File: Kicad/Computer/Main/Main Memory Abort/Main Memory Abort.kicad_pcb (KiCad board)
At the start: 2 copper layers, 18.8 x 43.3 mm, 14 parts, among them IC1 AP7365-33WG-7, IC2 74LVC32APW,118, IC4 74LVC74APW,118, IC5 SN74CBT3257CPWR, IC7 74LVC11PW,112, J2 Conn_02x16_Counter_Clockwise

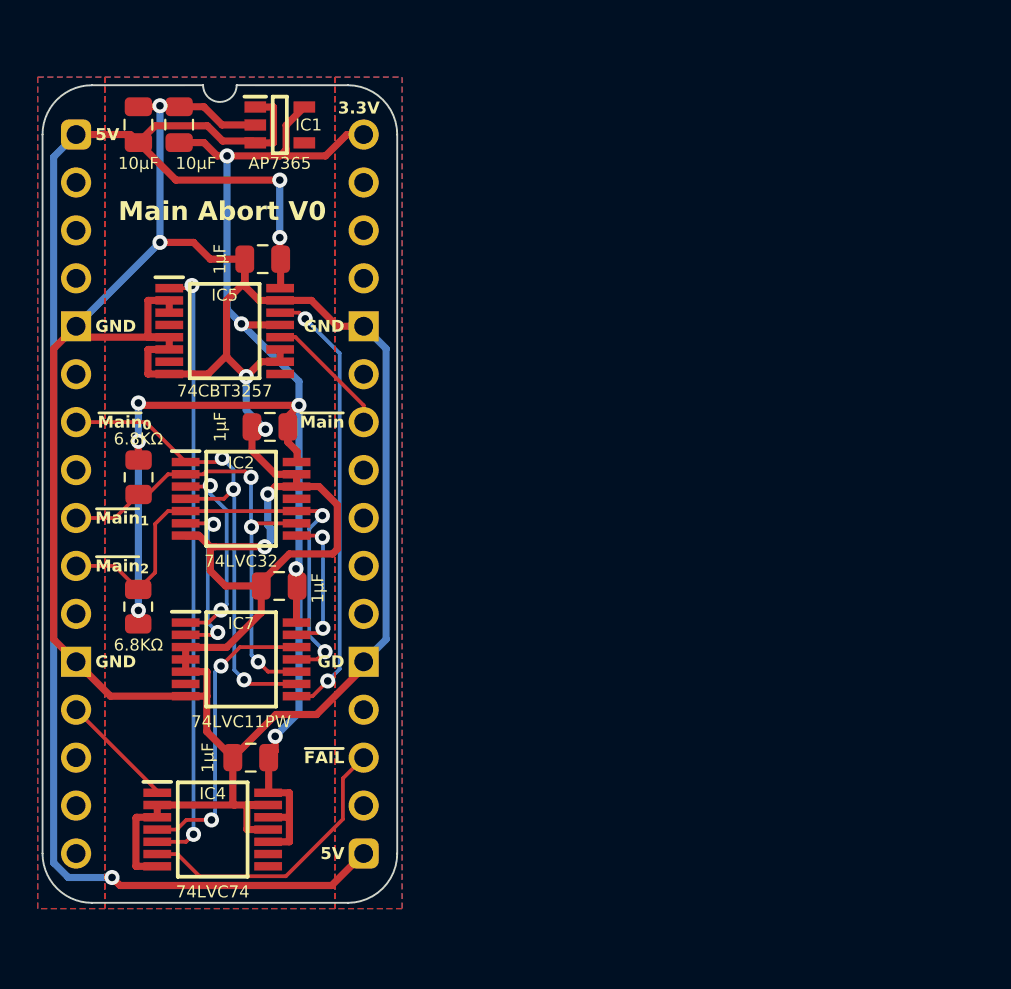
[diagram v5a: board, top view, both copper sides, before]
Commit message: Split Main Memory Abort into Enable and Abort.
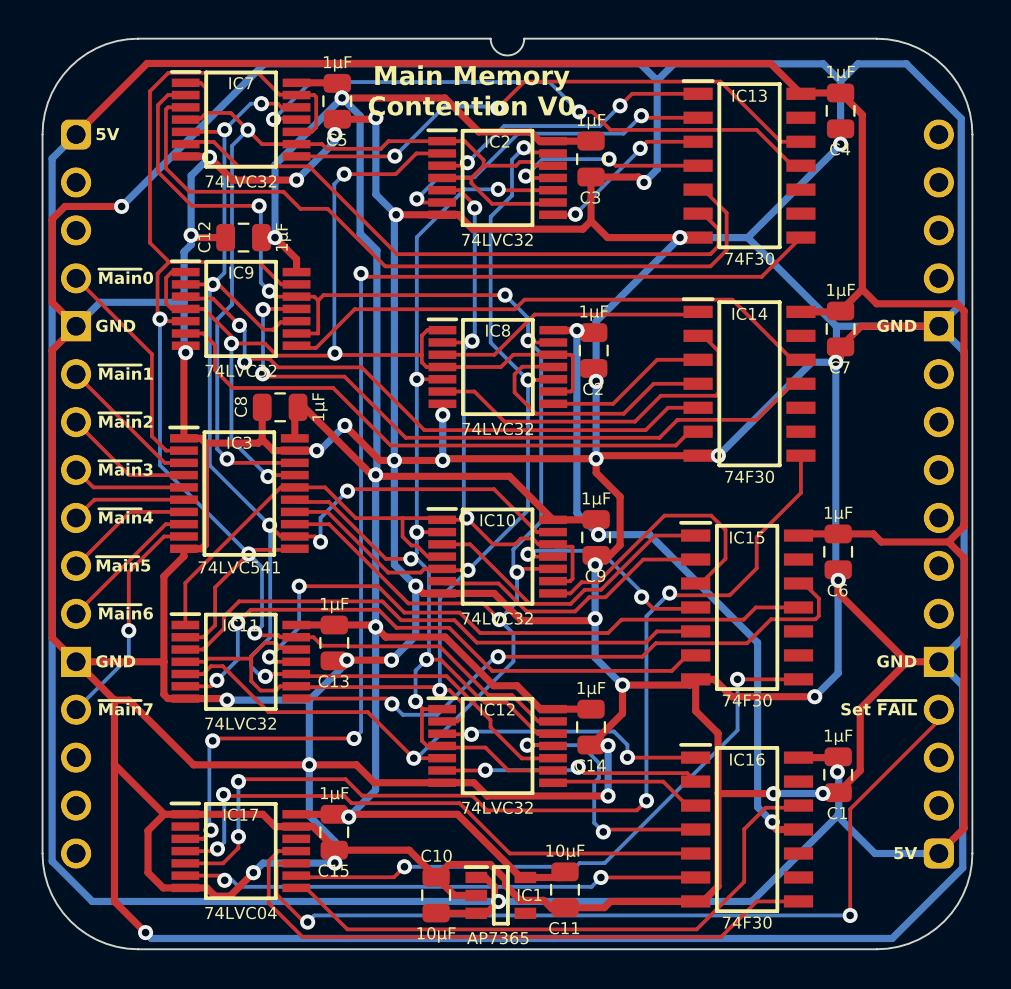
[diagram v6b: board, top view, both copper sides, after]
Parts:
- removed IC4: 74LVC74APW,118, SamacSys_Parts:SOP65P640X110-14N
- removed IC5: SN74CBT3257CPWR, SamacSys_Parts:SOP65P640X120-16N
- removed J2: Conn_02x16_Counter_Clockwise, SamacSys_Parts:DIP-32_Board_W15.24mm
- removed R1, R2: 6.8KΩ, SamacSys_Parts:R_0805
- added C1: 1μF, SamacSys_Parts:C_0805, F.Cu at (129.3, 92.3)
- added C12: 1μF, SamacSys_Parts:C_0805, F.Cu at (97.8, 63.9)
- added C13: 1μF, SamacSys_Parts:C_0805, F.Cu at (102.6, 85.3)
- added C14: 1μF, SamacSys_Parts:C_0805, F.Cu at (116.2, 89.8)
- added C15: 1μF, SamacSys_Parts:C_0805, F.Cu at (102.6, 95.4)
- added C6: 1μF, SamacSys_Parts:C_0805, F.Cu at (129.3, 80.5)
- added C7: 1μF, SamacSys_Parts:C_0805, F.Cu at (129.4, 68.7)
- added C8: 1μF, SamacSys_Parts:C_0805, F.Cu at (99.7, 72.9)
- added C9: 1μF, SamacSys_Parts:C_0805, F.Cu at (116.5, 79.8)
- added IC10: 74LVC32APW,118, SamacSys_Parts:SOP65P640X110-14N, F.Cu at (111.2, 80.8)
- added IC11: 74LVC32APW,118, SamacSys_Parts:SOP65P640X110-14N, F.Cu at (97.6, 86.4)
- added IC12: 74LVC32APW,118, SamacSys_Parts:SOP65P640X110-14N, F.Cu at (111.2, 90.8)
- added IC13: SN74F30DR, SamacSys_Parts:SOIC127P600X175-14N, F.Cu at (124.6, 60.1)
- added IC14: SN74F30DR, SamacSys_Parts:SOIC127P600X175-14N, F.Cu at (124.6, 71.6)
- added IC15: SN74F30DR, SamacSys_Parts:SOIC127P600X175-14N, F.Cu at (124.5, 83.5)
- added IC16: SN74F30DR, SamacSys_Parts:SOIC127P600X175-14N, F.Cu at (124.5, 95.2)
- added IC17: 74LVC04APW,118, SamacSys_Parts:SOP65P640X110-14N, F.Cu at (97.6, 96.4)
- added IC3: 74LVC541APW,118, SamacSys_Parts:SOP65P640X110-20N, F.Cu at (97.6, 77.4)
- added IC8: 74LVC32APW,118, SamacSys_Parts:SOP65P640X110-14N, F.Cu at (111.3, 70.7)
- added IC9: 74LVC32APW,118, SamacSys_Parts:SOP65P640X110-14N, F.Cu at (97.6, 67.7)
- added J1: Conn_01x16, SamacSys_Parts:SIP_16_Pins, F.Cu at (88.9, 58.4)
- added J3: Conn_01x16, SamacSys_Parts:SIP_16_Pins, F.Cu at (134.6, 96.5)
- IC7: value 74LVC11PW,112 -> 74LVC32APW,118
- moved C11 45.4 mm to (114.8, 98.4), turned to 180 degrees
- moved C10 43.8 mm to (108.0, 98.7)
- moved IC1 42.5 mm to (111.4, 98.7)
- moved C3 36.5 mm to (116.2, 59.7), turned to 180 degrees
- moved C4 31.6 mm to (129.4, 57.1), turned to 180 degrees
- moved IC7 28.6 mm to (97.6, 57.6)
- moved IC2 21.8 mm to (111.2, 60.7)
- moved C2 20.8 mm to (116.3, 69.8), turned to 180 degrees
- moved C5 17.6 mm to (102.7, 56.6), turned to 180 degrees
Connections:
- net 3.3V renamed /3.3V
- IC2 pad 1: ~{Main} -> /~{Main}B0
- IC2 pad 10: ~{Main}_{2} -> /~{Main}B3
- IC2 pad 11: unconnected-(IC2-4Y-Pad11) -> /~{0+4}
- IC2 pad 12: GND -> /~{Main}B0
- IC2 pad 13: GND -> /~{Main}B4
- IC2 pad 2: ~{Main}_{1} -> /~{Main}B1
- IC2 pad 3: /~{Main}+~{Main}_{1} -> /~{0+1}
- IC2 pad 4: ~{Main} -> /~{Main}B0
- IC2 pad 5: ~{Main}_{2} -> /~{Main}B2
- IC2 pad 6: /~{Main}+~{Main}_{2} -> /~{0+2}
- IC2 pad 8: /~{Main}_{1}+~{Main}_{2} -> /~{0+3}
- IC2 pad 9: ~{Main}_{1} -> /~{Main}B0
- IC7 pad 1: /~{Main}+~{Main}_{1} -> /~{Main}B0
- IC7 pad 10: ~{Main}_{1} -> /~{Main}B7
- IC7 pad 11: ~{Main}_{2} -> /~{6+7}
- IC7 pad 12: Net-(IC4-~{1SD}) -> /~{Main}B6
- IC7 pad 13: /~{Main}_{1}+~{Main}_{2} -> /~{Main}B7
- IC7 pad 2: /~{Main}+~{Main}_{2} -> /~{Main}B5
- IC7 pad 3: GND -> /~{0+5}
- IC7 pad 4: GND -> /~{Main}B0
- IC7 pad 5: GND -> /~{Main}B6
- IC7 pad 6: unconnected-(IC7-2Y-Pad6) -> /~{0+6}
- IC7 pad 8: Net-(IC5-4B1) -> /~{0+7}
- IC7 pad 9: ~{Main} -> /~{Main}B0
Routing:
- net GND: track 177.7 -> 589.0 mm, vias 6 -> 37
- net 5V: track 84.8 -> 201.6 mm, vias 3 -> 2
- net /~{Main}B5: track 0.00 -> 92.9 mm, vias 0 -> 7
- net /~{Main}B6: track 0.00 -> 80.5 mm, vias 0 -> 7
- net /~{Main}B7: track 0.00 -> 79.7 mm, vias 0 -> 3
- net /3.3V: track 85.2 -> 158.3 mm
- net /~{Main}B4: track 0.00 -> 67.2 mm, vias 0 -> 4
- net Net-(IC13-Y): track 0.00 -> 63.0 mm, vias 0 -> 4
- net /~{Main}B3: track 0.00 -> 63.0 mm, vias 0 -> 6
- net /~{Main}B1: track 0.00 -> 56.1 mm, vias 0 -> 4
- net /~{Main}B0: track 0.00 -> 53.3 mm, vias 0 -> 2
- net /~{Main}B2: track 0.00 -> 53.0 mm, vias 0 -> 3
- net Net-(IC14-Y): track 0.00 -> 52.9 mm, vias 0 -> 4
- net ~{Set Contention}: track 0.00 -> 46.1 mm, vias 0 -> 2
- net /~{0+5}: track 0.00 -> 40.2 mm
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- removed copper zone on B.Cu, net GND
- removed copper zone on F.Cu, net GND
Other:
- board size 18.8 x 43.3 mm -> 49.3 x 48.3 mm
- board text added: "Main Memory Contention V0"
- board text added: "Set ~{FAIL}"
- board text added: "~{Main}0"
- board text added: "~{Main}1"
- board text added: "~{Main}2"
- board text added: "~{Main}3"
- board text added: "~{Main}4"
- board text added: "~{Main}5"
- board text added: "~{Main}6"
- board text added: "~{Main}7"
- board text removed: "3.3V"
- board text removed: "GD"
- board text removed: "Main Abort V0"
- board text removed: "~{FAIL}"
- board text removed: "~{Main}"
- board text removed: "~{Main}_{0}"
- board text removed: "~{Main}_{1}"
- board text removed: "~{Main}_{2}"

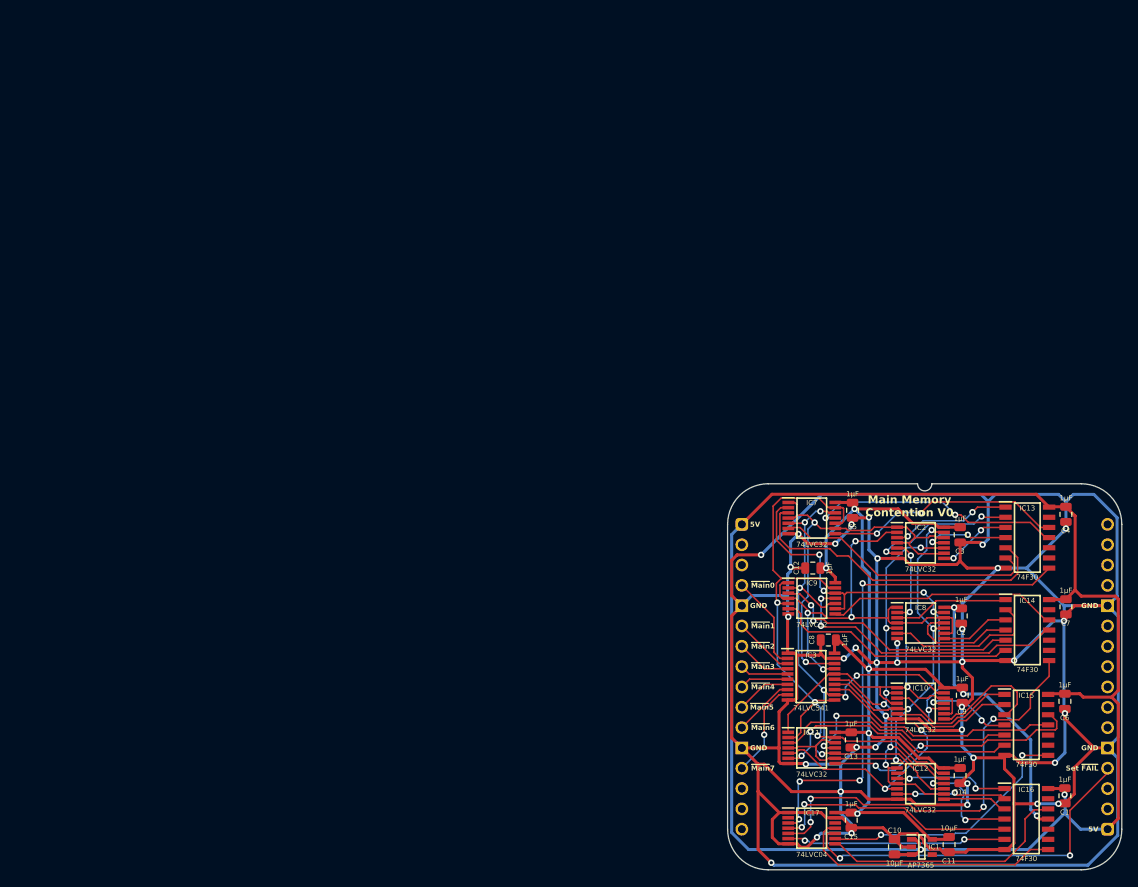
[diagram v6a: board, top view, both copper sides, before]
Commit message: Use VRML instead of STEPs for Main Board models.
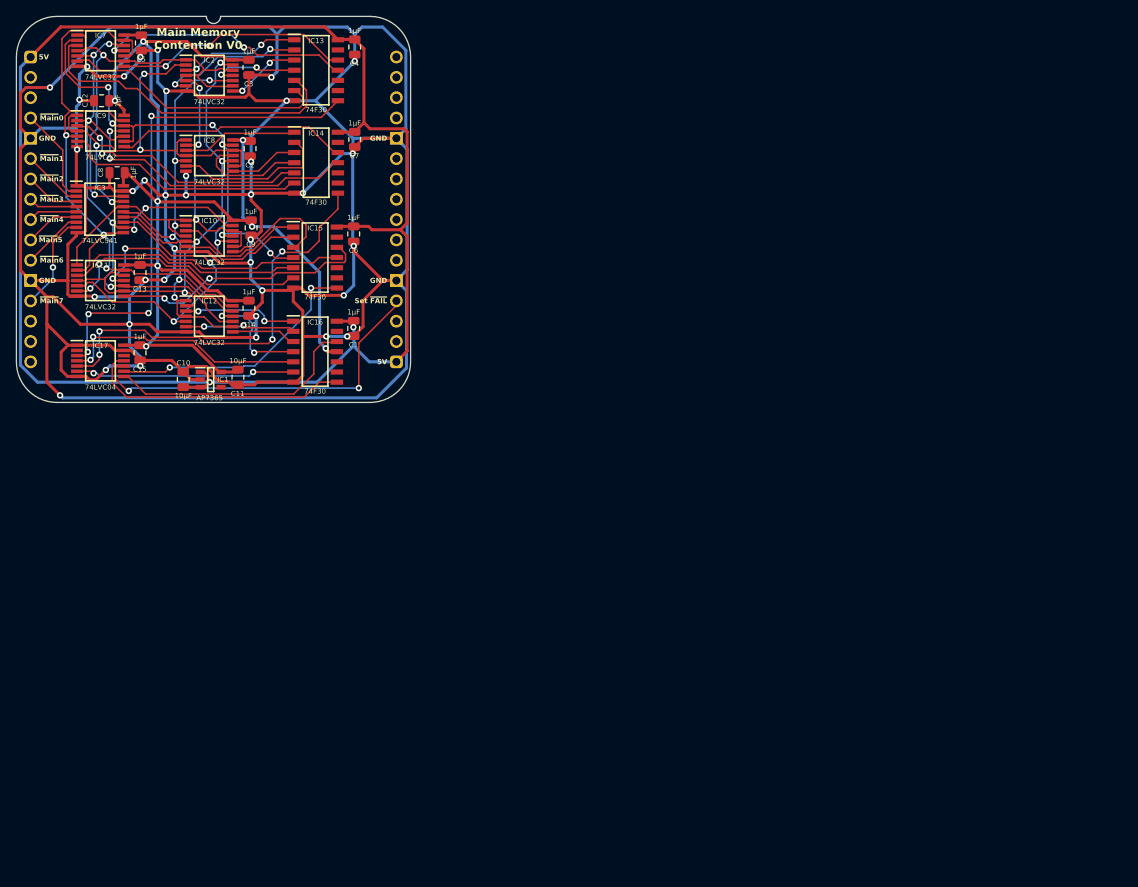
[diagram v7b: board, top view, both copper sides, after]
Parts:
- added J2: Pin_Header_01x16, SamacSys_Parts:PinHeader_1x16_P2.54mm_Vertical, B.Cu at (45.7, 0.00)
- added J4: Pin_Header_01x16, SamacSys_Parts:PinHeader_1x16_P2.54mm_Vertical, B.Cu at (0.00, 0.00)
- moved C1 106.4 mm to (40.4, 33.9)
- moved C10 106.4 mm to (19.1, 40.3)
- moved C11 106.4 mm to (25.9, 40.0)
- moved C12 106.4 mm to (8.89, 5.46)
- moved C14 106.4 mm to (27.3, 31.4)
- moved C3 106.4 mm to (27.3, 1.28)
- moved C4 106.4 mm to (40.5, -1.27)
- moved C6 106.4 mm to (40.4, 22.1)
- moved C7 106.4 mm to (40.5, 10.3)
- moved C8 106.4 mm to (10.8, 14.5)
- moved C9 106.4 mm to (27.6, 21.3)
- moved IC1 106.4 mm to (22.5, 40.3)
- moved IC10 106.4 mm to (22.3, 22.4)
- moved IC11 106.4 mm to (8.73, 27.9)
- moved IC12 106.4 mm to (22.3, 32.4)
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
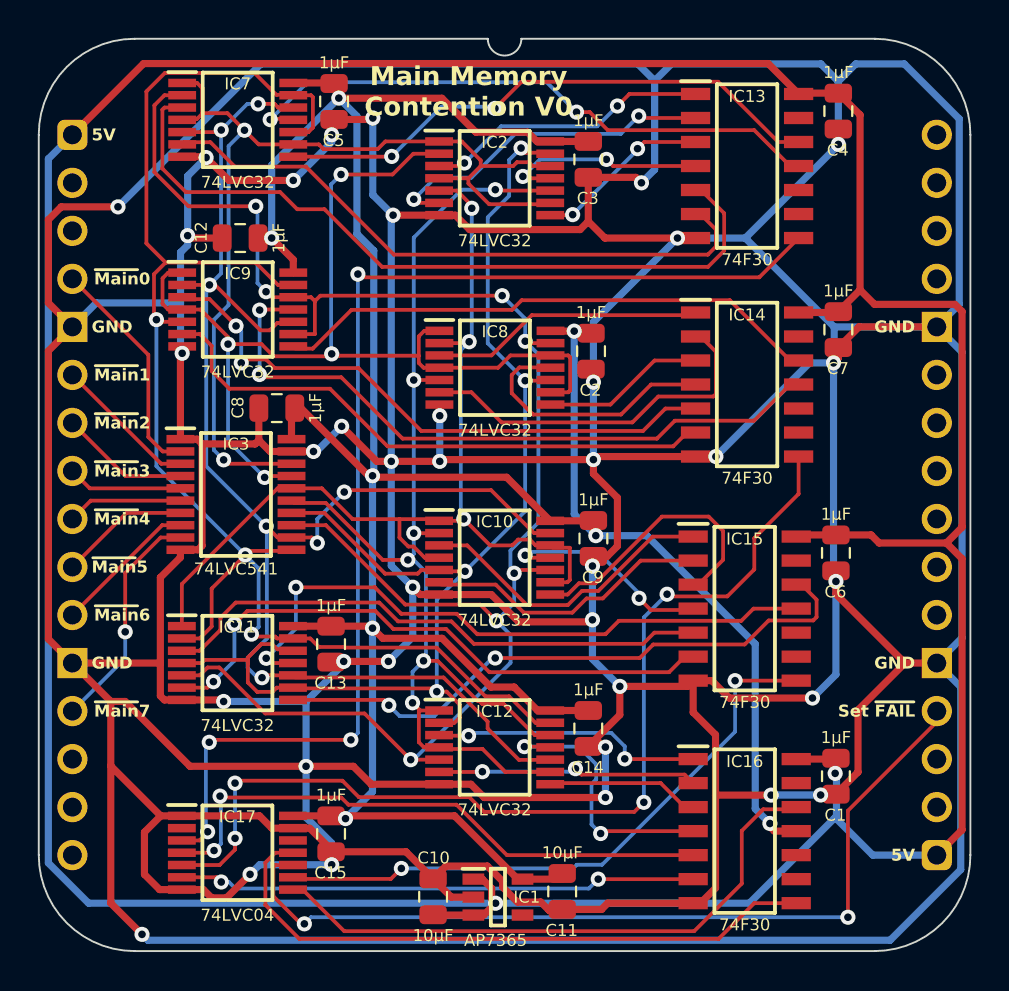
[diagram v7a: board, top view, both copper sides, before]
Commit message: Rounded Main Memory Abort traces.
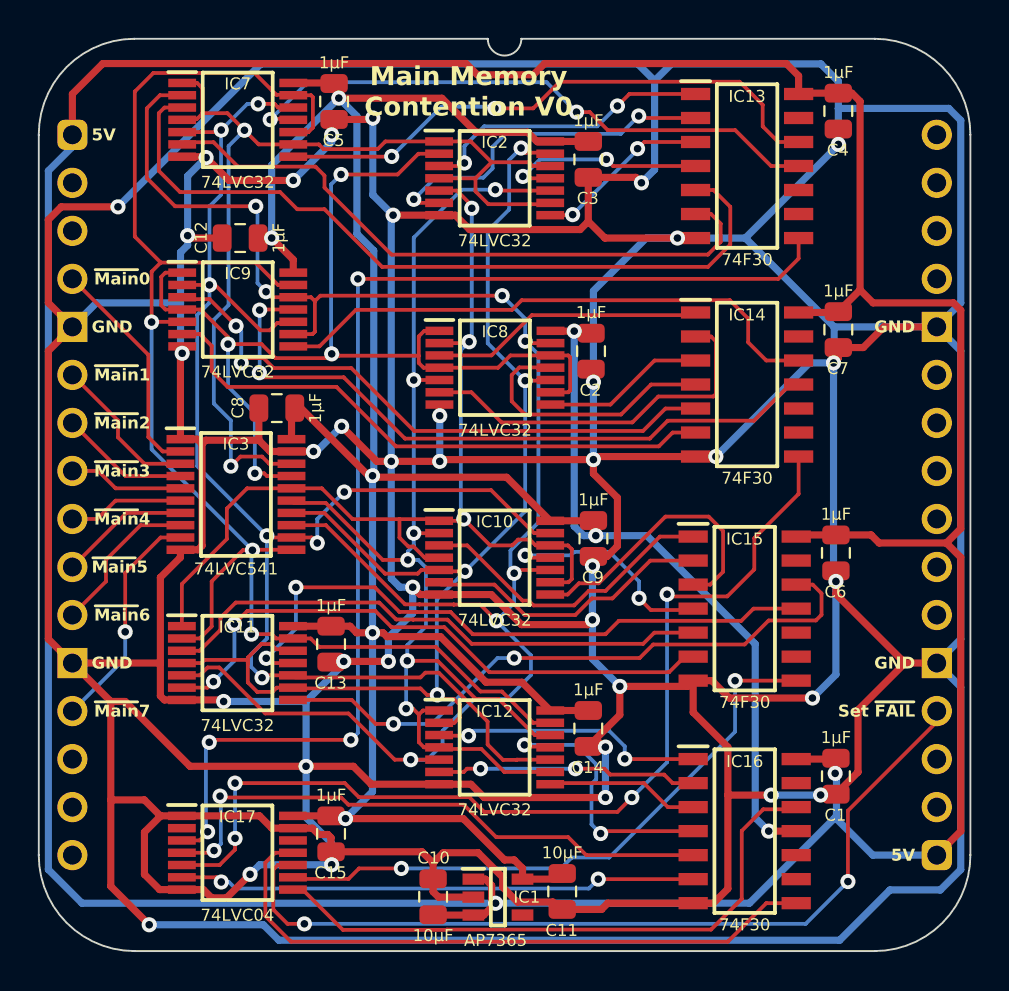
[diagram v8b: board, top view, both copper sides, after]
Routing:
- net /~{Main}B5: track 92.9 -> 96.0 mm
- net 5V: track 201.6 -> 204.5 mm
- net /~{Main}B3: track 63.0 -> 64.5 mm
- net GND: track 589.0 -> 590.3 mm
- net /~{4+6}: track 32.3 -> 33.5 mm
- net /~{5+6}: track 28.5 -> 29.8 mm
- net /~{Main}B2: track 53.0 -> 54.3 mm
- net /~{Main}B7: track 79.7 -> 80.8 mm
- net /3.3V: track 158.3 -> 159.3 mm
- net /~{0+5}: track 40.2 -> 41.1 mm
- net /~{0+6}: track 32.8 -> 33.7 mm
- net ~{Set Contention}: track 46.1 -> 45.3 mm
- net /~{0+2}: track 18.2 -> 18.9 mm
- net ~{Main}6: track 7.68 -> 8.35 mm
- net /~{0+7}: track 29.5 -> 30.1 mm
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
